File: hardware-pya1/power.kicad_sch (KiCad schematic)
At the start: 24 parts, among them Q1 AO3401A, Q2 BSS138, Q3 AO3401A, Q5 AO4953A, U1 LTC4054, U2 STI3411A, U5 XC6206PxxxMR

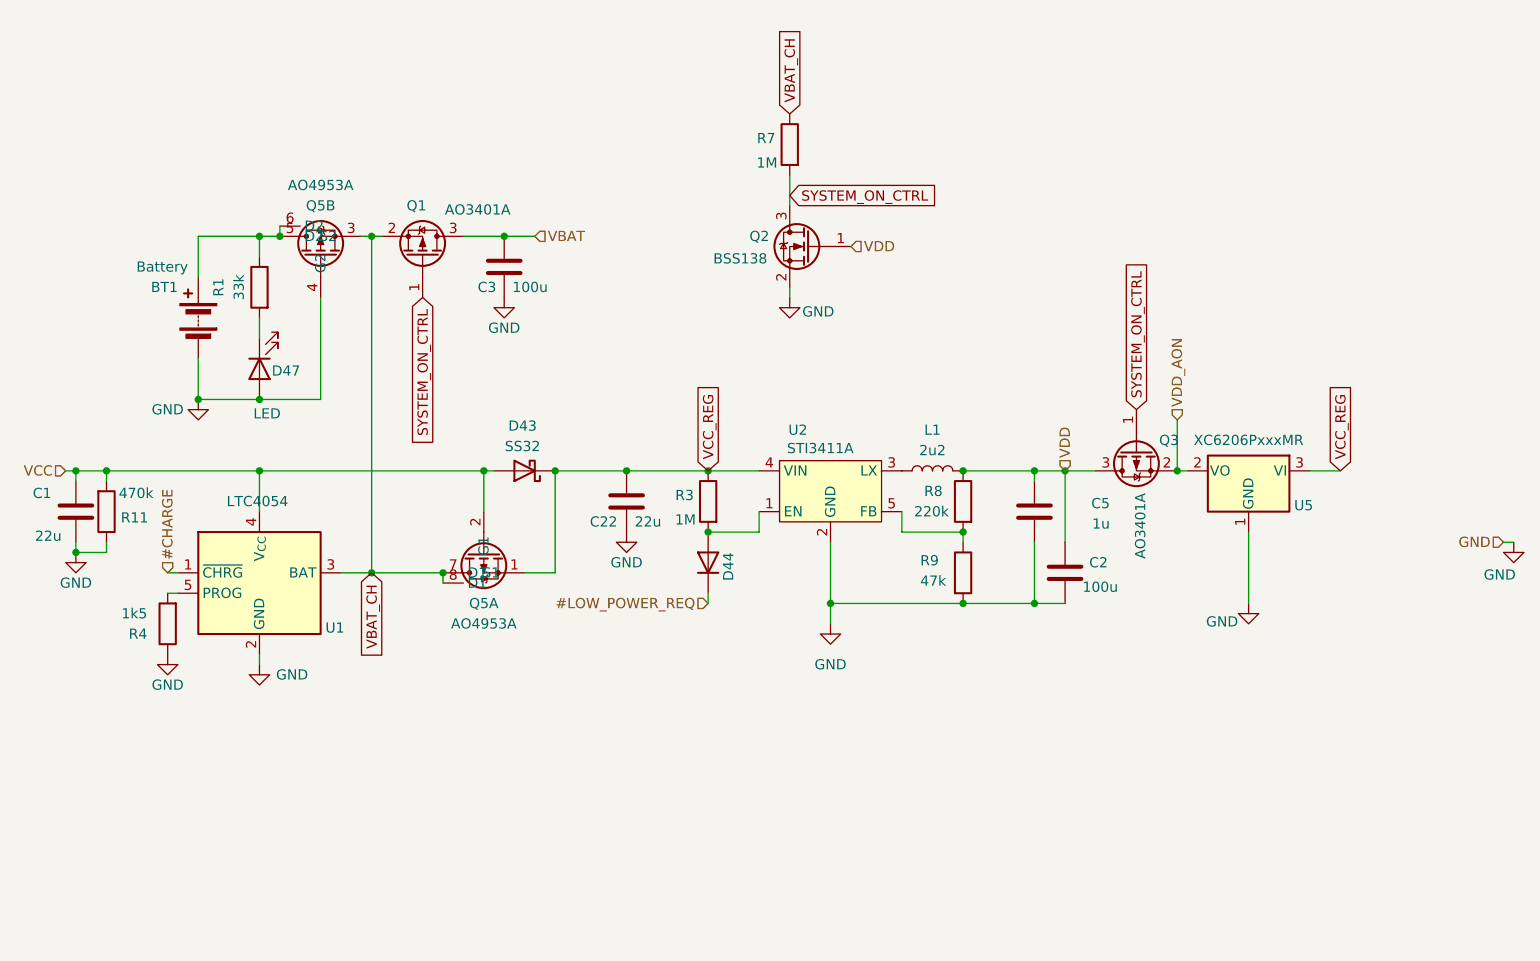
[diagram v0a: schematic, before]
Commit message: all: fix sleep in sw and hw but hw layout prevents keyscanning in sleep Need to find a way to sniff GPIO0 in sleep
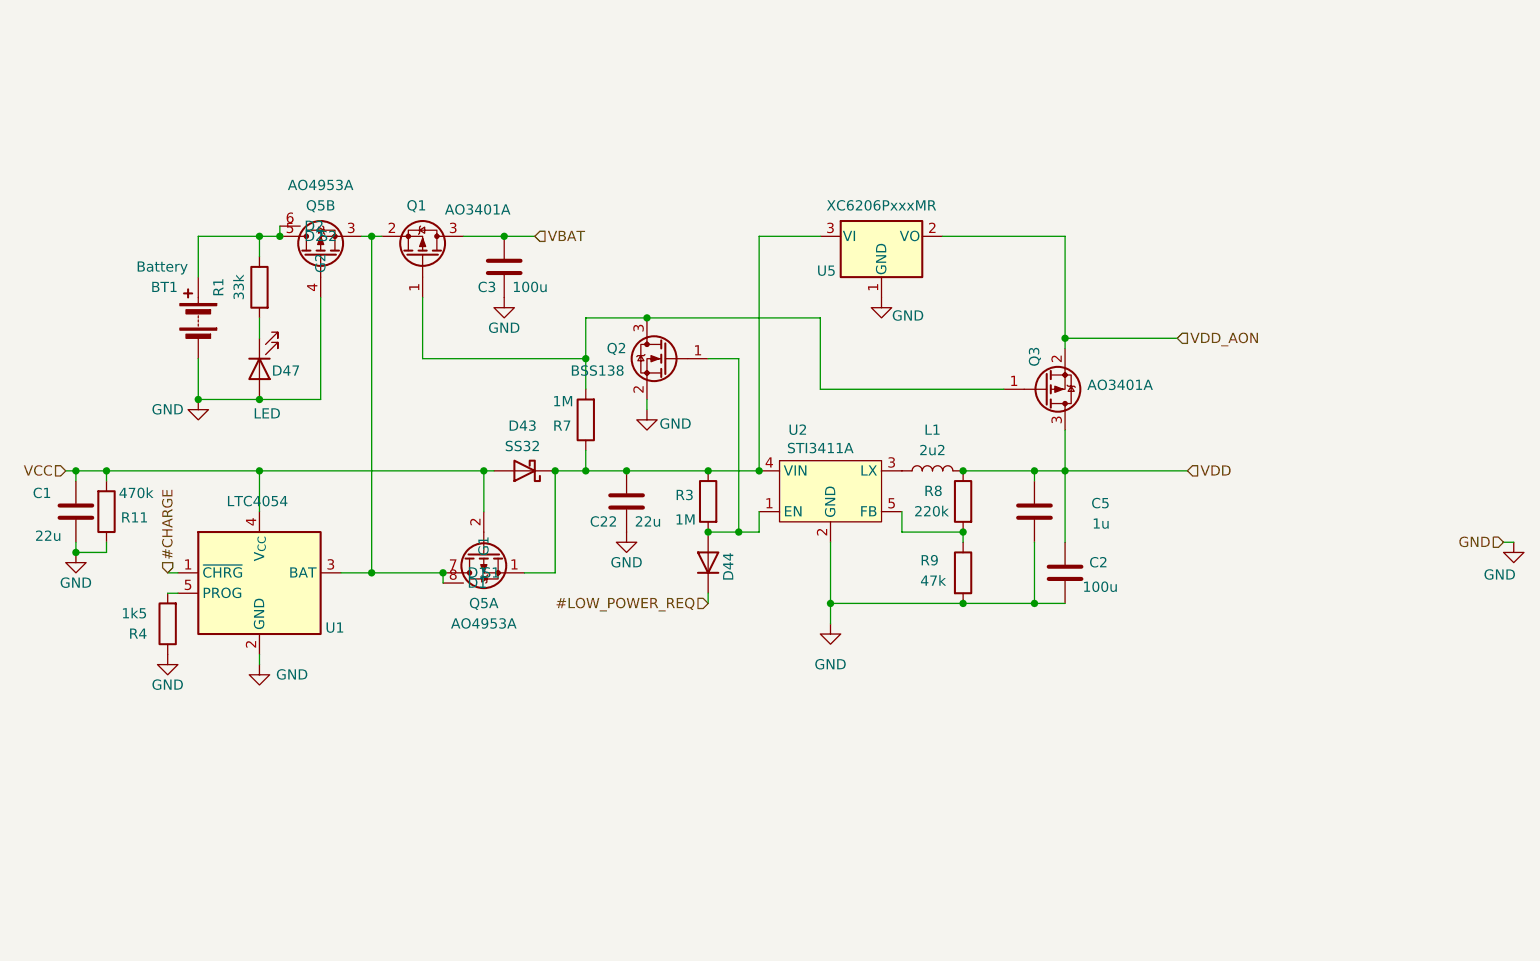
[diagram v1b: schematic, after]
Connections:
- net VDD: no longer Q2.1 (G)
- net at D44.2 (A), R3.2, U2.1 (EN): now also Q2.1 (G)
- net SYSTEM_ON_CTRL: no longer names the net of Q1.1 (G), Q2.3 (D), Q3.1 (G), R7.2
- net VBAT_CH: no longer names the net of Q1.2 (S), Q5.3 (S2), Q5.7 (D1), Q5.8 (D1), U1.3 (BAT)
- net VBAT_CH: no longer R7.1
- net VCC_REG: no longer names the net of C22.1, D43.1 (K), Q5.1 (S1), R3.1, U2.4 (VIN), U5.3 (VI)
- net VCC_REG: now also R7.1
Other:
- moved on the sheet: Q2, Q3, R7, U5

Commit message: pcb: redesign fix for LowPowerReq - added passives optional cap for slowstart on regulator switching to hi-power
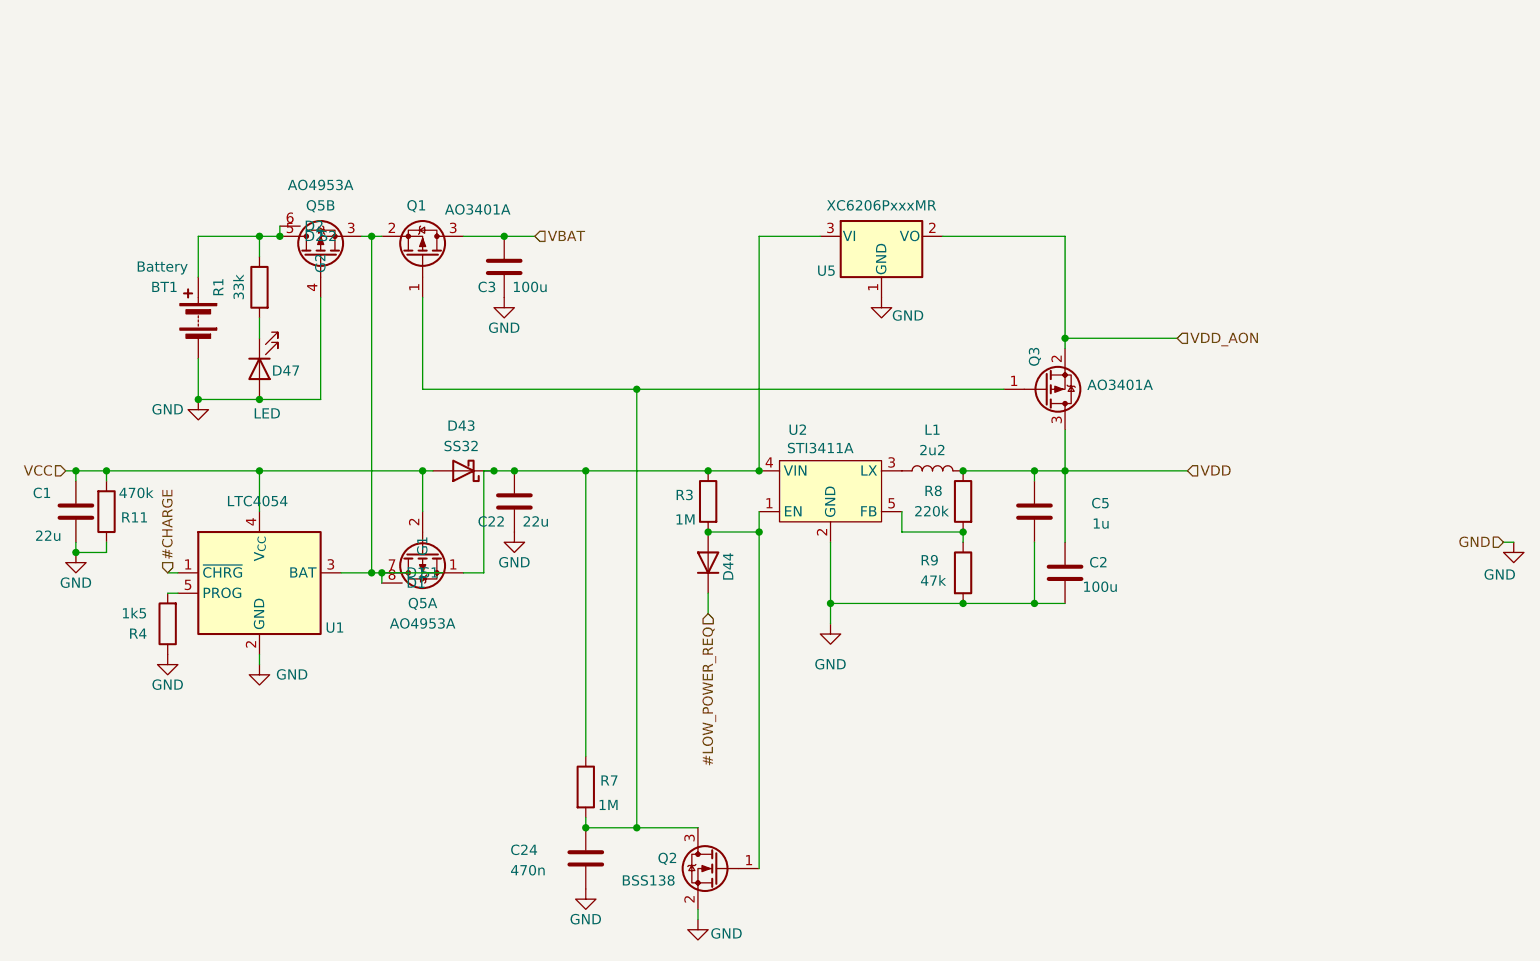
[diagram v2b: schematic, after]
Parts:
- added C24: 470n, Capacitor_SMD:C_0805_2012Metric_Pad1.18x1.45mm_HandSolder, symbol Device:C
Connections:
- net GND: now also C24.2
- net at Q1.1 (G), Q2.3 (D), Q3.1 (G)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: now also C24.1
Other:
- moved on the sheet: C22, D43, Q2, Q5A, R7

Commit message: pcb: revert led path to allow the option of populating rgb keys or not
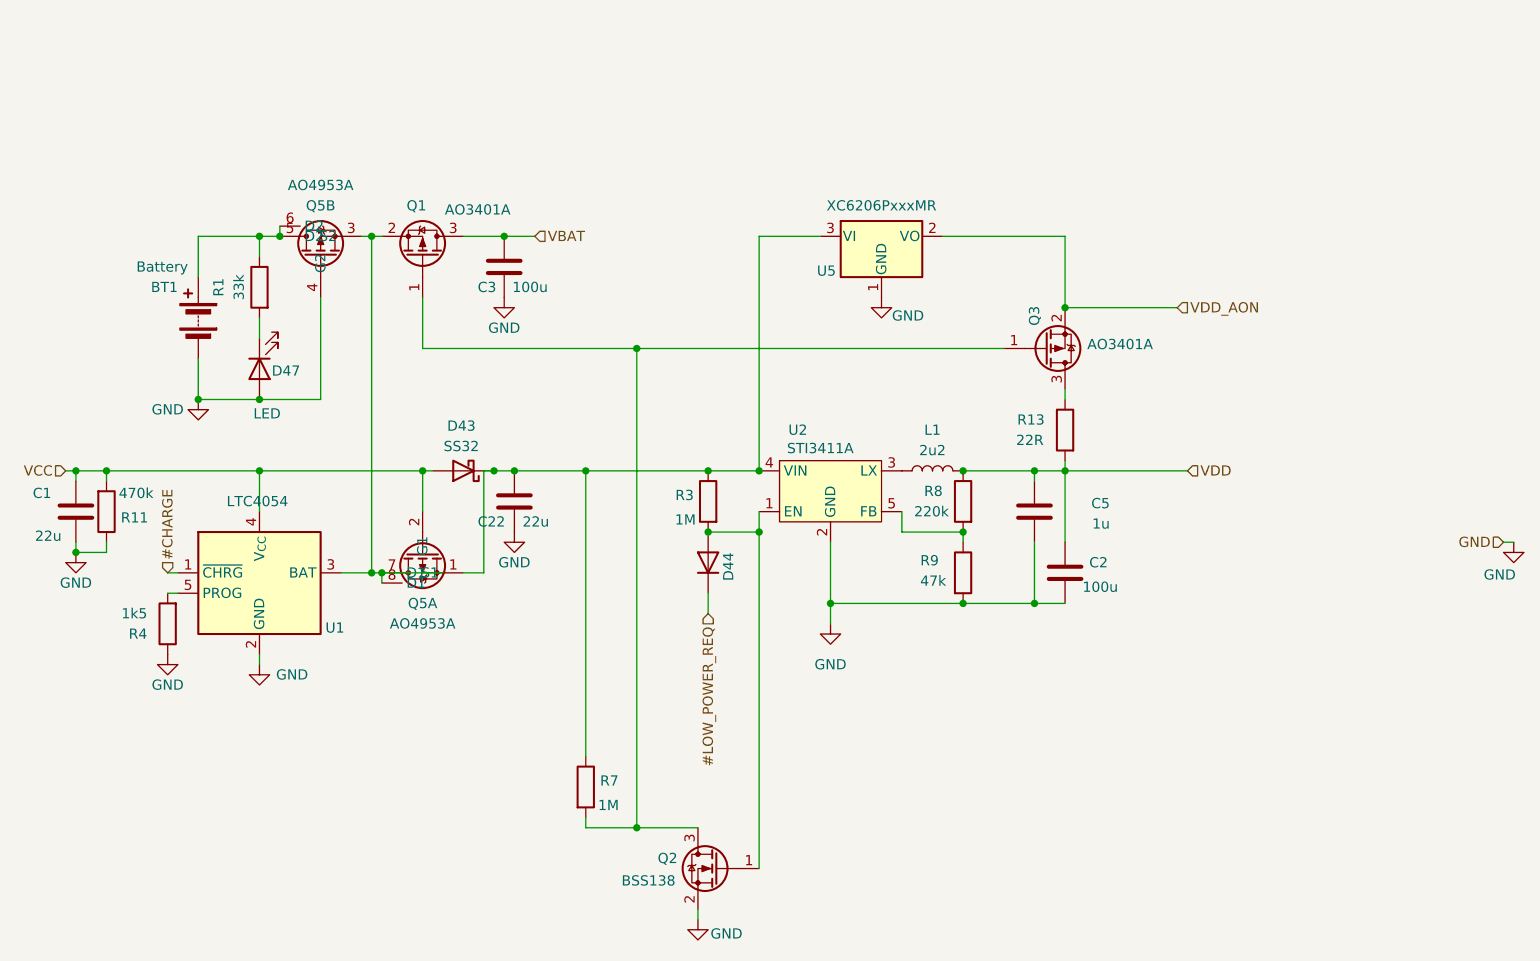
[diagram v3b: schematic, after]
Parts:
- removed C24: 470n, Capacitor_SMD:C_0805_2012Metric_Pad1.18x1.45mm_HandSolder, symbol Device:C
- added R13: 22R, Resistor_SMD:R_0805_2012Metric_Pad1.20x1.40mm_HandSolder, symbol Device:R
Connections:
- net VDD: now also R13.2; no longer Q3.3 (D)
- new net: Q3.3 (D), R13.1
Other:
- moved on the sheet: Q3
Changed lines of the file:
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@@
 	)
 	(junction
+		(at 130.81 93.98)
+		(diameter 0)
+		(color 0 0 0 0)
+	)
+	(junction
 		(at 130.81 153.67)
 		(diameter 0)
@@
 	)
 	(junction
-		(at 184.15 92.71)
-		(diameter 0)
-		(color 0 0 0 0)
-	)
-	(junction
 		(at 180.34 109.22)
 		(diameter 0)
@@
 	)
 	(junction
-		(at 60.96 119.38)
+		(at 184.15 88.9)
 		(diameter 0)
 		(color 0 0 0 0)
 	)
 	(junction
-		(at 124.46 153.67)
+		(at 60.96 119.38)
 		(diameter 0)
 		(color 0 0 0 0)
@@
 	)
 	(junction
-		(at 130.81 99.06)
-		(diameter 0)
-		(color 0 0 0 0)
-	)
-	(junction
 		(at 97.79 80.01)
 		(diameter 0)
@@
 	(wire
 		(pts
-			(xy 184.15 104.14) (xy 184.15 109.22)
+			(xy 163.83 114.3) (xy 163.83 116.84)
 		)
 		(stroke
@@
 	(wire
 		(pts
-			(xy 163.83 114.3) (xy 163.83 116.84)
+			(xy 184.15 107.95) (xy 184.15 109.22)
 		)
 		(stroke
@@
 	(wire
 		(pts
-			(xy 104.14 99.06) (xy 130.81 99.06)
+			(xy 104.14 93.98) (xy 130.81 93.98)
 		)
 		(stroke
@@
 	(wire
 		(pts
-			(xy 184.15 92.71) (xy 184.15 93.98)
-		)
-		(stroke
-			(width 0)
-			(type default)
-		)
-	)
-	(wire
-		(pts
-			(xy 184.15 80.01) (xy 184.15 92.71)
+			(xy 184.15 80.01) (xy 184.15 88.9)
 		)
 		(stroke
@@
 	(wire
 		(pts
-			(xy 104.14 87.63) (xy 104.14 99.06)
+			(xy 104.14 87.63) (xy 104.14 93.98)
 		)
 		(stroke
@@
 	(wire
 		(pts
-			(xy 130.81 99.06) (xy 176.53 99.06)
+			(xy 130.81 93.98) (xy 176.53 93.98)
 		)
 		(stroke
@@
 	(wire
 		(pts
-			(xy 184.15 92.71) (xy 198.12 92.71)
+			(xy 184.15 88.9) (xy 198.12 88.9)
 		)
 		(stroke
@@
 	(wire
 		(pts
-			(xy 130.81 99.06) (xy 130.81 153.67)
+			(xy 130.81 93.98) (xy 130.81 153.67)
 		)
 		(stroke
@@
 	(wire
 		(pts
+			(xy 184.15 99.06) (xy 184.15 100.33)
+		)
+		(stroke
+			(width 0)
+			(type default)
+		)
+	)
+	(wire
+		(pts
 			(xy 97.79 121.92) (xy 99.06 121.92)
 		)
@@
 	(hierarchical_label "VDD_AON"
 		(shape input)
-		(at 198.12 92.71 0)
+		(at 198.12 88.9 0)
 		(effects
 			(font
@@
 	(symbol
 		(lib_id "Transistor_FET:AO3401A")
-		(at 181.61 99.06 0)
+		(at 181.61 93.98 0)
 		(mirror x)
 		(unit 1)
@@
 		(dnp no)
 		(property "Reference" "Q3"
-			(at 180.34 94.996 90)
+			(at 180.34 89.916 90)
 			(effects
 				(font
@@
 		)
 		(property "Value" "AO3401A"
-			(at 191.008 98.552 0)
+			(at 191.008 93.472 0)
 			(effects
 				(font
@@
 		)
 		(property "Footprint" "Package_TO_SOT_SMD:SOT-23"
-			(at 186.69 97.155 0)
+			(at 186.69 92.075 0)
 			(effects
 				(font
@@
 		)
 		(property "Datasheet" "http://www.aosmd.com/pdfs/datasheet/AO3401A.pdf"
-			(at 181.61 99.06 0)
+			(at 181.61 93.98 0)
 			(effects
 				(font
@@
 		)
 		(property "Description" "-4.0A Id, -30V Vds, P-Channel MOSFET, SOT-23"
-			(at 181.61 99.06 0)
+			(at 181.61 93.98 0)
 			(effects
 				(font
@@
 	)
 	(symbol
-		(lib_id "power:GND")
-		(at 124.46 161.29 0)
+		(lib_id "Device:C")
+		(at 180.34 114.3 0)
+		(mirror y)
 		(unit 1)
 		(exclude_from_sim no)
@@
 		(on_board yes)
 		(dnp no)
-		(property "Reference" "#PWR21"
-			(at 124.46 167.64 0)
+		(property "Reference" "C5"
+			(at 189.738 113.284 0)
 			(effects
 				(font
 					(size 1.27 1.27)
 				)
-				(hide yes)
+				(justify left)
 			)
 		)
-		(property "Value" "GND"
-			(at 124.46 165.1 0)
+		(property "Value" "1u"
+			(at 189.738 115.824 0)
 			(effects
 				(font
 					(size 1.27 1.27)
 				)
+				(justify left)
 			)
 		)
-		(property "Footprint" ""
-			(at 124.46 161.29 0)
+		(property "Footprint" "Capacitor_SMD:C_0805_2012Metric_Pad1.18x1.45mm_HandSolder"
+			(at 179.3748 118.11 0)
 			(effects
 				(font
@@
 			)
 		)
-		(property "Datasheet" ""
-			(at 124.46 161.29 0)
+		(property "Datasheet" "~"
+			(at 180.34 114.3 0)
 			(effects
 				(font
@@
 			)
 		)
-		(property "Description" "Power symbol creates a global label with name \"GND\" , ground"
-			(at 124.46 161.29 0)
+		(property "Description" "Unpolarized capacitor"
+			(at 180.34 114.3 0)
 			(effects
 				(font
@@
 		(pin "1"
 		)
+		(pin "2"
+		)
 		(instances
 			(project "numcalcium"
 				(path "/842c0813-91d3-4f68-bc1f-ac3ce07be478/b6a1d74e-f5bd-4c1c-9567-b593baf30f34/94b3147a-b22b-4e06-91e3-a2640188c514"
-					(reference "#PWR21")
+					(reference "C5")
 					(unit 1)
 				)
@@
 	)
 	(symbol
-		(lib_id "Device:C")
-		(at 180.34 114.3 0)
+		(lib_id "Device:R")
+		(at 184.15 104.14 0)
 		(mirror y)
 		(unit 1)
@@
 		(on_board yes)
 		(dnp no)
-		(property "Reference" "C5"
-			(at 189.738 113.284 0)
+		(property "Reference" "R13"
+			(at 181.61 102.87 0)
 			(effects
 				(font
@@
 			)
 		)
-		(property "Value" "1u"
-			(at 189.738 115.824 0)
+		(property "Value" "22R"
+			(at 178.054 105.41 0)
 			(effects
 				(font
 					(size 1.27 1.27)
 				)
-				(justify left)
+				(justify right)
 			)
 		)
-		(property "Footprint" "Capacitor_SMD:C_0805_2012Metric_Pad1.18x1.45mm_HandSolder"
-			(at 179.3748 118.11 0)
+		(property "Footprint" "Resistor_SMD:R_0805_2012Metric_Pad1.20x1.40mm_HandSolder"
+			(at 185.928 104.14 90)
 			(effects
 				(font
@@
 		)
 		(property "Datasheet" "~"
-			(at 180.34 114.3 0)
+			(at 184.15 104.14 0)
 			(effects
 				(font
@@
 			)
 		)
-		(property "Description" "Unpolarized capacitor"
-			(at 180.34 114.3 0)
+		(property "Description" "Resistor"
+			(at 184.15 104.14 0)
 			(effects
 				(font
@@
 			)
 		)
-		(pin "1"
-		)
 		(pin "2"
 		)
+		(pin "1"
+		)
 		(instances
 			(project "numcalcium"
 				(path "/842c0813-91d3-4f68-bc1f-ac3ce07be478/b6a1d74e-f5bd-4c1c-9567-b593baf30f34/94b3147a-b22b-4e06-91e3-a2640188c514"
-					(reference "C5")
+					(reference "R13")
 					(unit 1)
 				)
@@
 					(unit 1)
 				)
-			)
-		)
-	)
-	(symbol
-		(lib_id "Device:C")
-		(at 124.46 157.48 0)
-		(unit 1)
-		(exclude_from_sim no)
-		(in_bom yes)
-		(on_board yes)
-		(dnp no)
-		(property "Reference" "C24"
-			(at 115.062 156.464 0)
-			(effects
-				(font
-					(size 1.27 1.27)
-				)
-				(justify left)
-			)
-		)
-		(property "Value" "470n"
-			(at 115.062 159.004 0)
-			(effects
-				(font
-					(size 1.27 1.27)
-				)
-				(justify left)
-			)
-		)
-		(property "Footprint" "Capacitor_SMD:C_0805_2012Metric_Pad1.18x1.45mm_HandSolder"
-			(at 125.4252 161.29 0)
-			(effects
-				(font
-					(size 1.27 1.27)
-				)
-				(hide yes)
-			)
-		)
-		(property "Datasheet" "~"
-			(at 124.46 157.48 0)
-			(effects
-				(font
-					(size 1.27 1.27)
-				)
-				(hide yes)
-			)
-		)
-		(property "Description" "Unpolarized capacitor"
-			(at 124.46 157.48 0)
-			(effects
-				(font
-					(size 1.27 1.27)
-				)
-				(hide yes)
-			)
-		)
-		(pin "1"
-		)
-		(pin "2"
-		)
-		(instances
-			(project "numcalcium"
-				(path "/842c0813-91d3-4f68-bc1f-ac3ce07be478/b6a1d74e-f5bd-4c1c-9567-b593baf30f34/94b3147a-b22b-4e06-91e3-a2640188c514"
-					(reference "C24")
-					(unit 1)
-				)
